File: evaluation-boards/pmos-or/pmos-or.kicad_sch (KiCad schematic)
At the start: 46 parts, among them J1 IN1, J10 GND, J2 IN2, J3 OUT, J4 USB_C_Receptacle_USB2.0, J5 USB_C_Receptacle_USB2.0, J6 USB_A, J7 IN1, J8 OUT, J9 IN2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

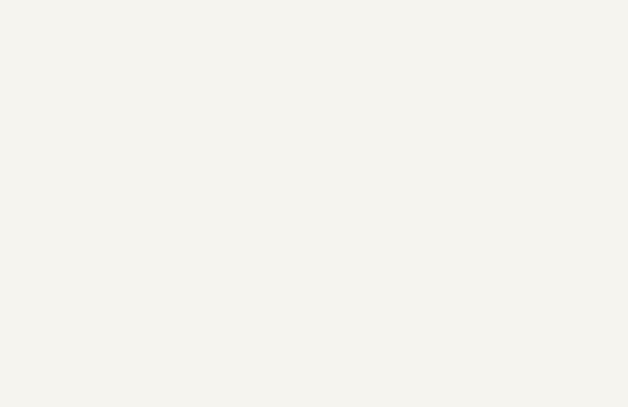
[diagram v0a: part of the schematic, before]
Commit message: pmos-or: add part selections
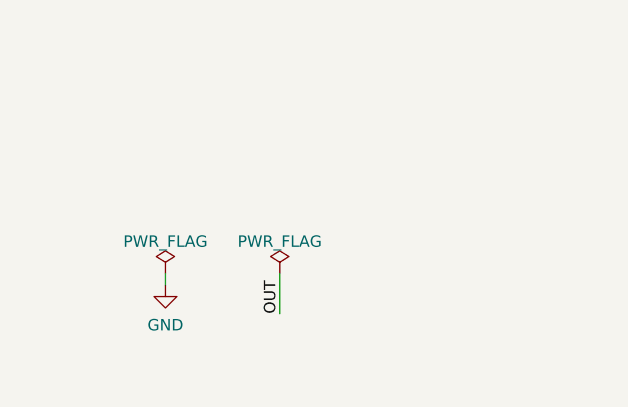
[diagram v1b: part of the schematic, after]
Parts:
- D1, D2: Manufacturer (none) -> Nexperia; Part Number (none) -> PMEG3050BEP,115
- J4, J5: Manufacturer (none) -> XKB; Part Number (none) -> U262-161N-4BVC11
- J6: Manufacturer (none) -> Jing Extension of the Electronic Co.; Part Number (none) -> C42411
- Q1, Q2, Q6: Manufacturer (none) -> Panjit; Part Number (none) -> PJA3441_R1_00001
- Q3: Manufacturer (none) -> Yangzhou Yangjie; Part Number (none) -> 2N7002DW
- Q4: Manufacturer (none) -> Diodes Inc.; Part Number (none) -> BCM857BS-7-F
- Q5: Manufacturer (none) -> Yangzhou Yangjie; Part Number (none) -> BSS84DW
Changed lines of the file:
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@@
+    (stroke (width 0) (type default) (color 0 0 0 0))
+  )
+  (wire (pts (xy 44.45 156.845) (xy 44.45 152.4))
     (stroke (width 0) (type default) (color 0 0 0 0))
   )
@@
   )
   (wire (pts (xy 163.83 46.99) (xy 163.83 52.07))
+    (stroke (width 0) (type default) (color 0 0 0 0))
+  )
+  (wire (pts (xy 31.75 152.4) (xy 31.75 153.67))
     (stroke (width 0) (type default) (color 0 0 0 0))
   )
@@
   )
   (label "G2" (at 207.01 63.5 0)
+    (effects (font (size 1.27 1.27)) (justify left bottom))
+  )
+  (label "OUT" (at 44.45 156.845 90)
     (effects (font (size 1.27 1.27)) (justify left bottom))
   )
@@
     )
     (property "DNP" "DNP" (id 4) (at 240.03 52.07 90))
+    (property "Manufacturer" "Nexperia" (id 5) (at 236.22 52.07 0)
+      (effects (font (size 1.27 1.27)) hide)
+    )
+    (property "Part Number" "PMEG3050BEP,115" (id 6) (at 236.22 52.07 0)
+      (effects (font (size 1.27 1.27)) hide)
+    )
     (pin "1")
     (pin "2")
@@
     )
     (property "Datasheet" "~" (id 3) (at 196.85 57.15 0)
+      (effects (font (size 1.27 1.27)) hide)
+    )
+    (property "Manufacturer" "Yangzhou Yangjie" (id 4) (at 195.58 57.15 0)
+      (effects (font (size 1.27 1.27)) hide)
+    )
+    (property "Part Number" "BSS84DW" (id 5) (at 195.58 57.15 0)
       (effects (font (size 1.27 1.27)) hide)
     )
@@
       (effects (font (size 1.27 1.27)) hide)
     )
+    (property "Manufacturer" "Diodes Inc." (id 4) (at 196.85 88.265 0)
+      (effects (font (size 1.27 1.27)) hide)
+    )
+    (property "Part Number" "BCM857BS-7-F" (id 5) (at 196.85 88.265 0)
+      (effects (font (size 1.27 1.27)) hide)
+    )
     (pin "1")
     (pin "2")
@@
     (pin "2")
   )
+  (symbol (lib_id "power:GND") (at 31.75 153.67 0) (mirror y) (unit 1)
+    (in_bom yes) (on_board yes) (fields_autoplaced)
+    (property "Reference" "#PWR0107" (id 0) (at 31.75 160.02 0)
+      (effects (font (size 1.27 1.27)) hide)
+    )
+    (property "Value" "GND" (id 1) (at 31.75 158.1134 0))
+    (property "Footprint" "" (id 2) (at 31.75 153.67 0)
+      (effects (font (size 1.27 1.27)) hide)
+    )
+    (property "Datasheet" "" (id 3) (at 31.75 153.67 0)
+      (effects (font (size 1.27 1.27)) hide)
+    )
+    (pin "1")
+  )
   (symbol (lib_id "power:GND") (at 227.33 92.075 0) (mirror y) (unit 1)
     (in_bom yes) (on_board yes) (fields_autoplaced)
@@
     )
     (property "Datasheet" "https://www.usb.org/sites/default/files/documents/usb_type-c.zip" (id 3) (at 264.16 126.365 0)
+      (effects (font (size 1.27 1.27)) hide)
+    )
+    (property "Manufacturer" "XKB" (id 4) (at 267.97 126.365 0)
+      (effects (font (size 1.27 1.27)) hide)
+    )
+    (property "Part Number" "U262-161N-4BVC11" (id 5) (at 267.97 126.365 0)
       (effects (font (size 1.27 1.27)) hide)
     )
@@
       (effects (font (size 1.27 1.27)) hide)
     )
+    (property "Manufacturer" "Yangzhou Yangjie" (id 4) (at 172.72 63.5 0)
+      (effects (font (size 1.27 1.27)) hide)
+    )
+    (property "Part Number" "2N7002DW" (id 5) (at 172.72 63.5 0)
+      (effects (font (size 1.27 1.27)) hide)
+    )
     (pin "1")
     (pin "2")
@@
       (effects (font (size 1.27 1.27)) hide)
     )
+    (property "Manufacturer" "Yangzhou Yangjie" (id 4) (at 93.98 57.15 0)
+      (effects (font (size 1.27 1.27)) hide)
+    )
+    (property "Part Number" "BSS84DW" (id 5) (at 93.98 57.15 0)
+      (effects (font (size 1.27 1.27)) hide)
+    )
     (pin "1")
     (pin "2")
@@
       (effects (font (size 1.27 1.27)) hide)
     )
+    (property "Manufacturer" "Panjit" (id 4) (at 214.63 63.5 0)
+      (effects (font (size 1.27 1.27)) hide)
+    )
+    (property "Part Number" "PJA3441_R1_00001" (id 5) (at 214.63 63.5 0)
+      (effects (font (size 1.27 1.27)) hide)
+    )
     (pin "1")
     (pin "2")
@@
     )
     (property "Datasheet" "~" (id 3) (at 184.15 88.265 0)
+      (effects (font (size 1.27 1.27)) hide)
+    )
+    (property "Manufacturer" "Diodes Inc." (id 4) (at 184.15 88.265 0)
+      (effects (font (size 1.27 1.27)) hide)
+    )
+    (property "Part Number" "BCM857BS-7-F" (id 5) (at 184.15 88.265 0)
       (effects (font (size 1.27 1.27)) hide)
     )
@@
     (pin "2")
   )
+  (symbol (lib_id "power:PWR_FLAG") (at 44.45 152.4 0) (unit 1)
+    (in_bom yes) (on_board yes) (fields_autoplaced)
+    (property "Reference" "#FLG0102" (id 0) (at 44.45 150.495 0)
+      (effects (font (size 1.27 1.27)) hide)
+    )
+    (property "Value" "PWR_FLAG" (id 1) (at 44.45 148.8242 0))
+    (property "Footprint" "" (id 2) (at 44.45 152.4 0)
+      (effects (font (size 1.27 1.27)) hide)
+    )
+    (property "Datasheet" "~" (id 3) (at 44.45 152.4 0)
+      (effects (font (size 1.27 1.27)) hide)
+    )
+    (pin "1")
+  )
   (symbol (lib_id "Device:R") (at 181.61 100.33 0) (mirror y) (unit 1)
     (in_bom yes) (on_board yes) (fields_autoplaced)
@@
       (effects (font (size 1.27 1.27)) hide)
     )
+    (property "Manufacturer" "Jing Extension of the Electronic Co." (id 4) (at 22.86 27.94 0)
+      (effects (font (size 1.27 1.27)) hide)
+    )
+    (property "Part Number" "C42411" (id 5) (at 22.86 27.94 0)
+      (effects (font (size 1.27 1.27)) hide)
+    )
     (pin "1")
     (pin "2")
@@
     )
     (property "DNP" "DNP" (id 4) (at 148.59 52.07 90))
+    (property "Manufacturer" "Nexperia" (id 5) (at 144.78 52.07 0)
+      (effects (font (size 1.27 1.27)) hide)
+    )
+    (property "Part Number" "PMEG3050BEP,115" (id 6) (at 144.78 52.07 0)
+      (effects (font (size 1.27 1.27)) hide)
+    )
     (pin "1")
     (pin "2")
@@
     )
     (property "Datasheet" "~" (id 3) (at 111.76 63.5 0)
+      (effects (font (size 1.27 1.27)) hide)
+    )
+    (property "Manufacturer" "Panjit" (id 4) (at 111.76 63.5 0)
+      (effects (font (size 1.27 1.27)) hide)
+    )
+    (property "Part Number" "PJA3441_R1_00001" (id 5) (at 111.76 63.5 0)
       (effects (font (size 1.27 1.27)) hide)
     )
@@
     )
     (property "Datasheet" "~" (id 3) (at 70.485 109.855 0)
+      (effects (font (size 1.27 1.27)) hide)
+    )
+    (property "Manufacturer" "Yangzhou Yangjie" (id 4) (at 65.405 109.855 0)
+      (effects (font (size 1.27 1.27)) hide)
+    )
+    (property "Part Number" "2N7002DW" (id 5) (at 65.405 109.855 0)
       (effects (font (size 1.27 1.27)) hide)
     )
@@
     (pin "5")
   )
+  (symbol (lib_id "power:PWR_FLAG") (at 31.75 152.4 0) (unit 1)
+    (in_bom yes) (on_board yes) (fields_autoplaced)
+    (property "Reference" "#FLG0101" (id 0) (at 31.75 150.495 0)
+      (effects (font (size 1.27 1.27)) hide)
+    )
+    (property "Value" "PWR_FLAG" (id 1) (at 31.75 148.8242 0))
+    (property "Footprint" "" (id 2) (at 31.75 152.4 0)
+      (effects (font (size 1.27 1.27)) hide)
+    )
+    (property "Datasheet" "~" (id 3) (at 31.75 152.4 0)
+      (effects (font (size 1.27 1.27)) hide)
+    )
+    (pin "1")
+  )
   (symbol (lib_id "power:GND") (at 260.985 46.355 0) (unit 1)
     (in_bom yes) (on_board yes) (fields_autoplaced)
@@
     )
     (property "Datasheet" "~" (id 3) (at 166.37 57.15 0)
+      (effects (font (size 1.27 1.27)) hide)
+    )
+    (property "Manufacturer" "Panjit" (id 4) (at 166.37 57.15 0)
+      (effects (font (size 1.27 1.27)) hide)
+    )
+    (property "Part Number" "PJA3441_R1_00001" (id 5) (at 166.37 57.15 0)
       (effects (font (size 1.27 1.27)) hide)
     )
@@
     )
     (property "Datasheet" "https://www.usb.org/sites/default/files/documents/usb_type-c.zip" (id 3) (at 115.57 123.19 0)
+      (effects (font (size 1.27 1.27)) hide)
+    )
+    (property "Manufacturer" "XKB" (id 4) (at 111.76 123.19 0)
+      (effects (font (size 1.27 1.27)) hide)
+    )
+    (property "Part Number" "U262-161N-4BVC11" (id 5) (at 111.76 123.19 0)
       (effects (font (size 1.27 1.27)) hide)
     )
@@
   )
   (symbol_instances
+    (path "/d4edca07-ef56-467e-a371-d404f86d5ea7"
+      (reference "#FLG0101") (unit 1) (value "PWR_FLAG") (footprint "")
+    )
+    (path "/b83ff5c1-9c87-49a5-a183-18ef906b50d5"
+      (reference "#FLG0102") (unit 1) (value "PWR_FLAG") (footprint "")
+    )
     (path "/bde3c2f9-8b67-47c3-ba7a-1580461cb493"
       (reference "#PWR01") (unit 1) (value "GND") (footprint "")
@@
       (reference "#PWR0106") (unit 1) (value "GND") (footprint "")
     )
+    (path "/6f6b4e26-b6a9-45a9-b364-aee5ed2b3257"
+      (reference "#PWR0107") (unit 1) (value "GND") (footprint "")
+    )
     (path "/ad80e6b3-18d3-4983-89a7-9086dfc6ecea"

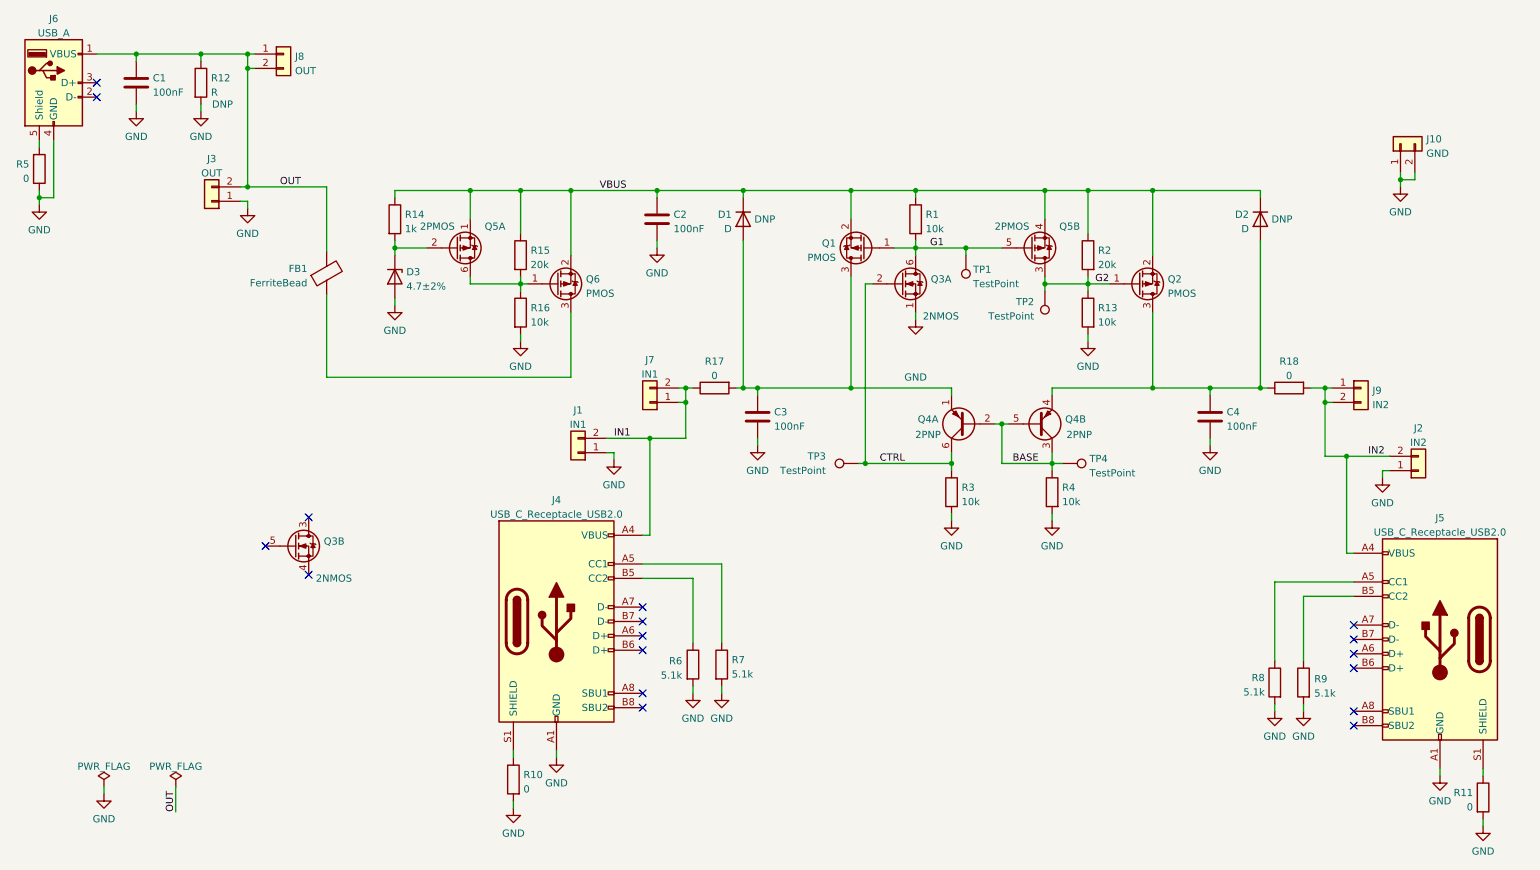
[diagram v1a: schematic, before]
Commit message: update CONSMA003.062 footprint
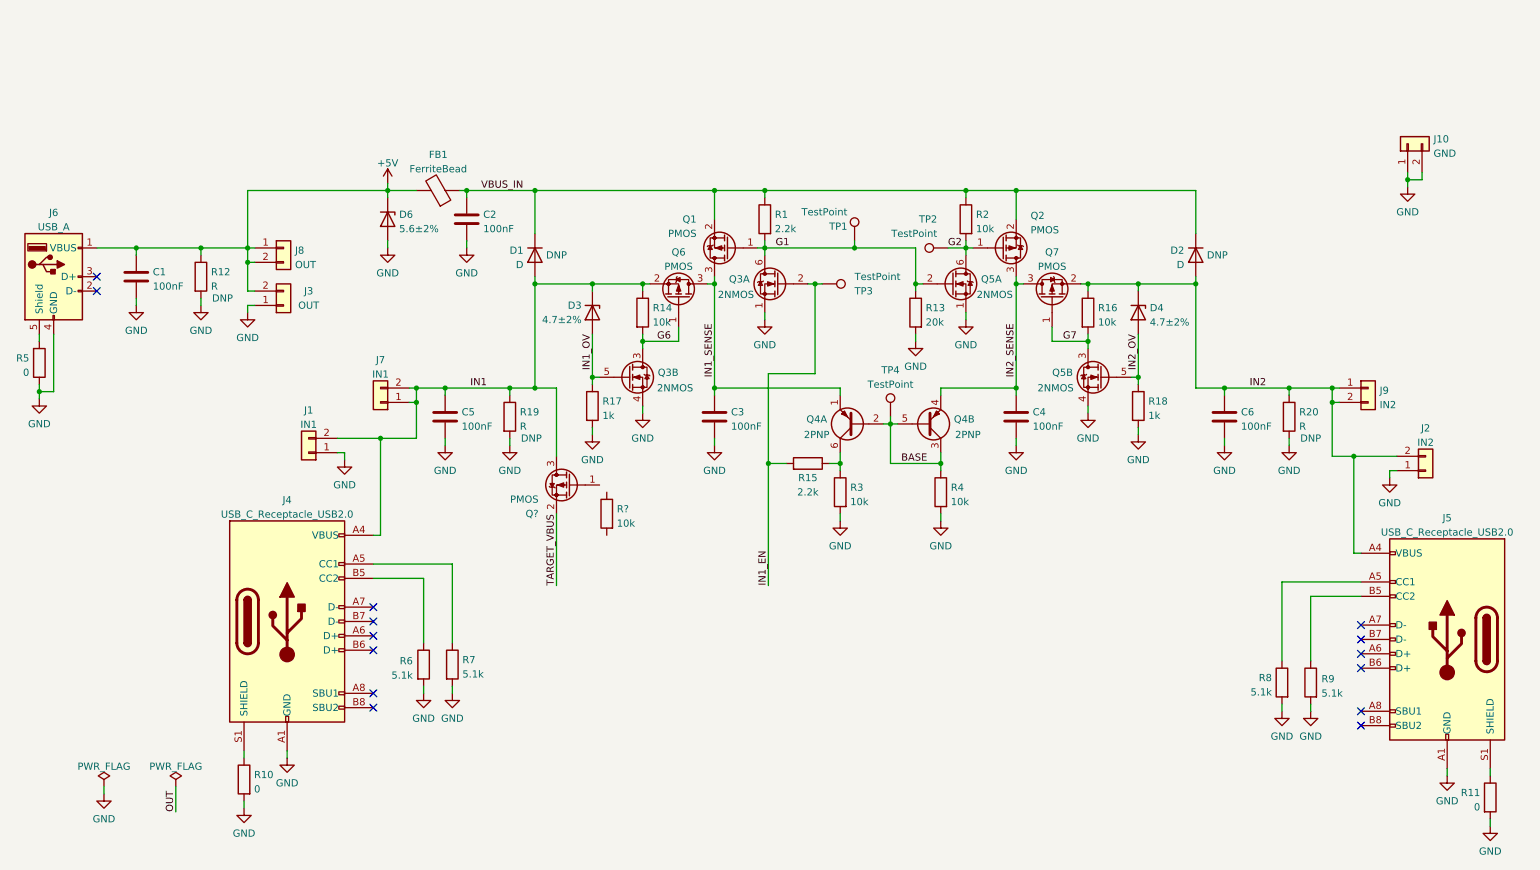
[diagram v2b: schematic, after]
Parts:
- removed Q5: 2PMOS, Package_TO_SOT_SMD:SOT-363_SC-70-6, symbol Device:Q_Dual_PMOS_S1G1D2S2G2D1
- added C5, C6: 100nF, Capacitor_SMD:C_0402_1005Metric, symbol Device:C
- added D4: 4.7±2%, eval:DFN1006-2, symbol Device:D_Zener
- added D6: 5.6±2%, eval:DFN1006-2, symbol Device:D_Zener
- added Q5: 2NMOS, Package_TO_SOT_SMD:SOT-363_SC-70-6, symbol Device:Q_Dual_NMOS_S1G1D2S2G2D1
- added Q7, Q?: PMOS, Package_TO_SOT_SMD:SOT-23-3, symbol Device:Q_PMOS_GSD
- added R19, R20: R, Resistor_SMD:R_0402_1005Metric, symbol Device:R
- added R?: 10k, Resistor_SMD:R_0402_1005Metric, symbol Device:R
- R1: value 10k -> 2.2k
- R13: value 10k -> 20k
- R14: value 1k -> 10k
- R15: value 20k -> 2.2k
- R17, R18: value 0 -> 1k
- R2: value 20k -> 10k
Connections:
- net G1: now also R13.1, Q5.2 (G)
- net G2: now also Q5.6 (D); no longer R13.1
- net GND: now also Q3.4 (S), R17.2, R18.2, C5.2, C6.2, D6.2 (A), Q5.1 (S), Q5.4 (S), R19.2, R20.2; no longer D3.2 (A), R16.2
- net IN1: now also D1.2 (A), D3.1 (K), Q6.2 (S), R14.1, C5.1, Q?.3 (D), R19.1; no longer R17.1
- net IN2: now also D2.2 (A), R16.1, C6.1, D4.1 (K), Q7.2 (S), R20.1; no longer R18.2
- net OUT: no longer C1.1, FB1.2, J3.2 (Pin_2), J6.1 (VBUS), J8.1 (Pin_1), J8.2 (Pin_2), R12.1
- net IN2_SENSE: now reaches C4.1, Q2.3 (D), Q4.4 (E2)
- net IN2_SENSE: now also Q7.3 (D); no longer D2.2 (A), R18.1
- net G6: now reaches R14.2
- net G6: now also Q3.3 (D), Q6.1 (G); no longer D3.1 (K)
- net IN1_SENSE: now reaches Q6.3 (D)
- net IN1_SENSE: now also C3.1, Q1.3 (D), Q4.1 (E1); no longer FB1.1
- net IN1_OV: now reaches Q3.5 (G)
- net IN1_OV: now also D3.2 (A), R17.1
- net CTRL: no longer names the net of Q4.6 (C1), R3.1
- net CTRL: now also R15.1; no longer Q3.2 (G), TP3.1
- net VBUS renamed VBUS_IN
- net VBUS_IN: now also FB1.1; no longer Q6.2 (S), R14.1, R15.1
- new net +5V: C1.1, D6.1 (K), FB1.2, J3.2 (Pin_2), J6.1 (VBUS), J8.1 (Pin_1), J8.2 (Pin_2), R12.1
- new net G7: Q5.3 (D), Q7.1 (G), R16.2
- new net IN1_EN: Q3.2 (G), R15.2, TP3.1
- new net IN2_OV: D4.2 (A), Q5.5 (G), R18.1
- new net TARGET_VBUS: Q?.2 (S)
- no-connect marks 17 -> 14
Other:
- moved on the sheet: C1, C2, C3, C4, D1, D2, FB1, J1, J10, J2, J3, J4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
